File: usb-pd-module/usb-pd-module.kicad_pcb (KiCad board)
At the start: 2 copper layers, 34.3 x 46.3 mm, 33 parts, among them J1 USBC, J2 OUT, U1 CH221K, U2 SPX1117M3

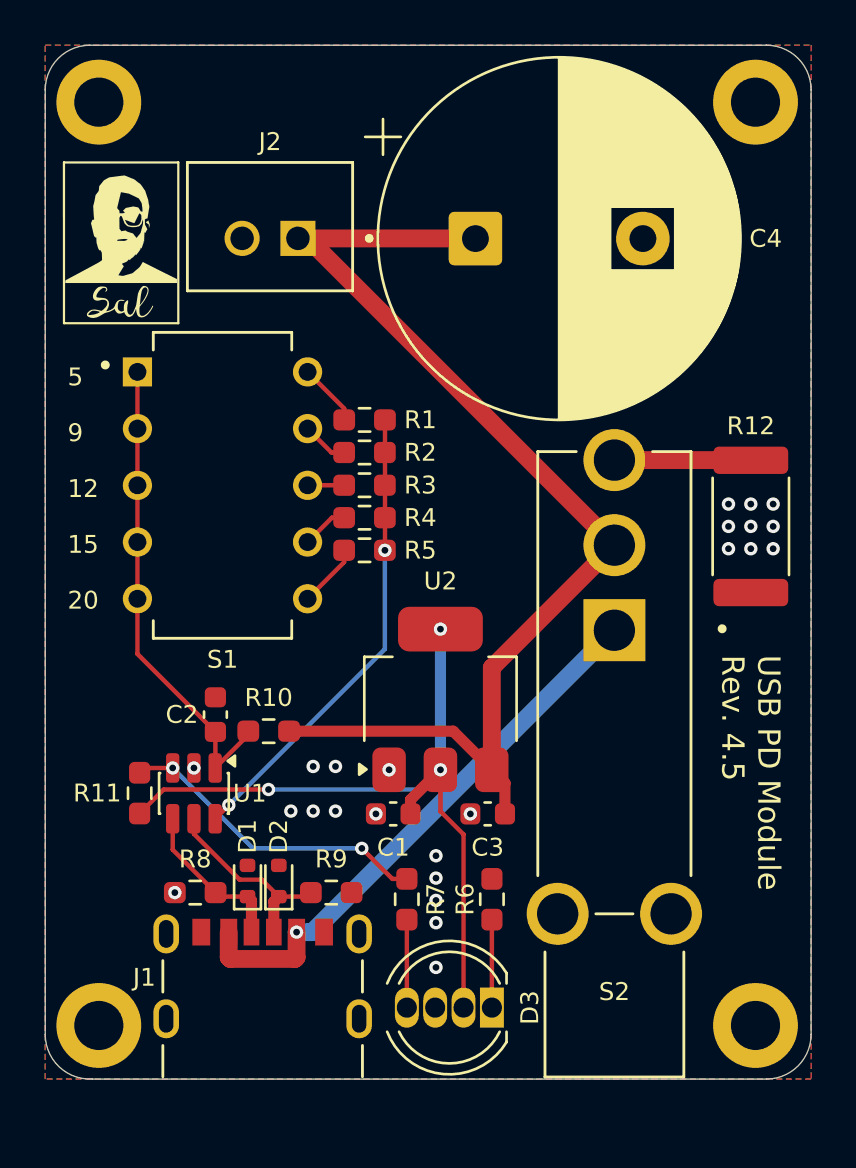
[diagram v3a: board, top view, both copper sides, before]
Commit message: Adjust USB-C connector and main switch placement for better enclosure compatibility
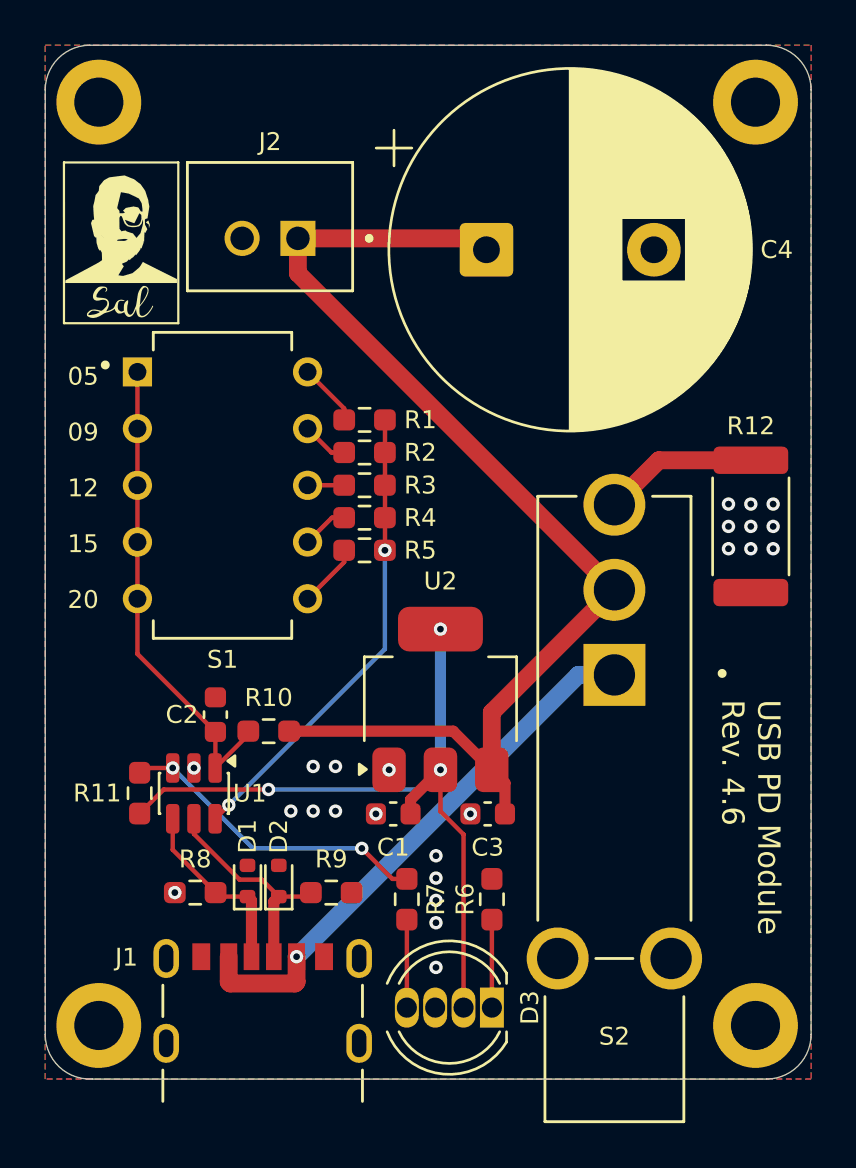
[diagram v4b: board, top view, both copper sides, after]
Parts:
- moved REF** 2.00 mm to (59.6, 76.2)
- moved REF** 2.00 mm to (50.6, 76.0)
- moved S2 2.00 mm to (60.5, 66.1)
- moved J1 1.10 mm to (44.7, 85.5)
- moved C4 0.70 mm to (54.8, 50.9)
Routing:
- net CC1: track 7.27 -> 8.37 mm
- net CC2: track 8.84 -> 9.94 mm
- net BLEED: track 6.11 -> 6.95 mm
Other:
- board text added: "05"
- board text added: "09"
- board text added: "USB PD Module Rev. 4.6"
- board text removed: "5"
- board text removed: "9"
- board text removed: "USB PD Module Rev. 4.5"
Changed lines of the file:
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@@
 	(title_block
 		(title "USB PD Module PCB")
-		(date "2026-03-21")
-		(rev "4.5")
+		(date "2026-05-27")
+		(rev "4.6")
 		(company "Salinder Sidhu")
 	)
@@
 	(footprint "footprints:SW_100SP1T2B4M7QE"
 		(layer "F.Cu")
-		(at 60.49 64.09 90)
+		(at 60.49 66.09 90)
 		(property "Reference" "S2"
 			(at -20 0 180)
@@
 	(footprint "footprints:AMPHENOL_10164359-00011LF"
 		(layer "F.Cu")
-		(at 44.7375 84.45)
+		(at 44.7375 85.55)
 		(property "Reference" "J1"
-			(at -5.3 -1 0)
+			(at -6.1 -3 0)
 			(layer "F.SilkS")
 			(effects
@@
 	(footprint "Capacitor_THT:CP_Radial_D16.0mm_P7.50mm"
 		(layer "F.Cu")
-		(at 54.267246 50.36)
+		(at 54.76 50.86)
 		(descr "CP, Radial series, Radial, pin pitch=7.50mm, diameter=16mm, height=25mm, Electrolytic Capacitor")
 		(tags "CP Radial series Radial pin pitch 7.50mm diameter 16mm height 25mm Electrolytic Capacitor")
@@
 	(footprint "Symbol:WEEE-Logo_4.2x6mm_SilkScreen"
 		(layer "B.Cu")
-		(at 59.57 74.21 180)
+		(at 59.57 76.21 180)
 		(descr "Waste Electrical and Electronic Equipment Directive https://eur-lex.europa.eu/legal-content/EN/TXT/PDF/?uri=CELEX:32012L0019#page=29")
 		(tags "Logo WEEE")
@@
 	(footprint "Symbol:KiCad-Logo2_5mm_SilkScreen"
 		(layer "B.Cu")
-		(at 50.57 73.96 180)
+		(at 50.57 75.96 180)
 		(descr "KiCad Logo")
 		(tags "Logo KiCad")
@@
 		(layer "Edge.Cuts")
 	)
-	(gr_text "5"
-		(at 36 57.03 0)
+	(gr_text "05"
+		(at 36 57 0)
 		(layer "F.SilkS")
 		(effects
@@
 		)
 	)
-	(gr_text "9"
-		(at 36 59.53 0)
+	(gr_text "09"
+		(at 36 59.5 0)
 		(layer "F.SilkS")
 		(effects
@@
 	)
 	(gr_text "12"
-		(at 36 62.03 0)
+		(at 36 62 0)
 		(layer "F.SilkS")
 		(effects
@@
 	)
 	(gr_text "15"
-		(at 36 64.53 0)
+		(at 36 64.5 0)
 		(layer "F.SilkS")
 		(effects
@@
 	)
 	(gr_text "20"
-		(at 36 67.03 0)
+		(at 36 67 0)
 		(layer "F.SilkS")
 		(effects
@@
 		)
 	)
-	(gr_text "USB PD Module\nRev. 4.5"
-		(at 65.2 69 270)
+	(gr_text "USB PD Module\nRev. 4.6"
+		(at 65.2 71 270)
 		(layer "F.SilkS")
 		(effects
@@
 	)
 	(segment
+		(start 45.2375 82.52)
+		(end 45.2375 80.0525)
+		(width 0.5)
+		(layer "F.Cu")
+		(net "CC2")
+	)
+	(segment
 		(start 46.7175 79.83)
 		(end 46.8975 79.65)
@@
 	)
 	(segment
-		(start 41.66 77.021968)
-		(end 41.66 76.34375)
-		(width 0.2)
+		(start 45.2375 80.0525)
+		(end 45.46 79.83)
+		(width 0.5)
 		(layer "F.Cu")
 		(net "CC2")
 	)
 	(segment
-		(start 45.2375 81.42)
-		(end 45.2375 80.0525)
-		(width 0.5)
+		(start 41.66 77.021968)
+		(end 41.66 76.34375)
+		(width 0.2)
 		(layer "F.Cu")
 		(net "CC2")
@@
 		(net "CC2")
 	)
-	(segment
-		(start 45.2375 80.0525)
-		(end 45.46 79.83)
-		(width 0.5)
-		(layer "F.Cu")
-		(net "CC2")
-	)
 	(via
 		(at 50.4 74.15)
@@
 	)
 	(segment
-		(start 46.2575 81.42)
-		(end 46.2575 82.552)
+		(start 46.2575 83.65)
+		(end 46.1875 83.72)
 		(width 0.8)
 		(layer "F.Cu")
@@
 	)
 	(segment
-		(start 43.2175 82.552)
-		(end 43.2175 81.42)
+		(start 46.2575 82.52)
+		(end 46.2575 83.65)
 		(width 0.8)
 		(layer "F.Cu")
@@
 	)
 	(segment
-		(start 43.2865 82.621)
-		(end 43.2175 82.552)
+		(start 43.2875 83.72)
+		(end 43.2175 83.65)
 		(width 0.8)
 		(layer "F.Cu")
@@
 	)
 	(segment
-		(start 46.1885 82.621)
-		(end 43.2865 82.621)
+		(start 43.2175 83.65)
+		(end 43.2175 82.52)
 		(width 0.8)
 		(layer "F.Cu")
@@
 	)
 	(segment
-		(start 46.2575 82.552)
-		(end 46.1885 82.621)
+		(start 46.1875 83.72)
+		(end 43.2875 83.72)
 		(width 0.8)
 		(layer "F.Cu")
@@
 	)
 	(via
-		(at 46.2575 81.42)
+		(at 46.2575 82.52)
 		(size 0.6)
 		(drill 0.3)
 		(layers "F.Cu" "B.Cu")
-		(capping no)
-		(covering
-			(front no)
-			(back no)
-		)
-		(plugging
-			(front no)
-			(back no)
-		)
-		(filling no)
 		(net "VBUS")
 	)
 	(segment
-		(start 46.2575 81.42)
-		(end 46.97 81.42)
+		(start 58.8775 69.9)
+		(end 60.49 69.9)
 		(width 0.8)
 		(layer "B.Cu")
@@
 	)
 	(segment
-		(start 46.97 81.42)
-		(end 60.49 67.9)
+		(start 46.2575 82.52)
+		(end 58.8775 69.9)
 		(width 0.8)
 		(layer "B.Cu")
@@
 	)
 	(segment
-		(start 47 50.6)
-		(end 47 50.35)
+		(start 54.25 50.35)
+		(end 54.76 50.86)
+		(width 0.8)
+		(layer "F.Cu")
+		(net "PWR")
+	)
+	(segment
+		(start 46.3175 51.9175)
+		(end 60.49 66.09)
 		(width 0.8)
 		(layer "F.Cu")
@@
 	)
 	(segment
-		(start 60.49 64.09)
-		(end 46.75 50.35)
+		(start 60.49 66.09)
+		(end 55 71.58)
 		(width 0.8)
 		(layer "F.Cu")
@@
 	)
 	(segment
-		(start 55 69.58)
-		(end 55 74.15)
+		(start 46.3175 50.35)
+		(end 46.3175 51.9175)
 		(width 0.8)
 		(layer "F.Cu")
@@
 	)
 	(segment
-		(start 46.75 50.35)
-		(end 46.3175 50.35)
+		(start 46.3175 50.35)
+		(end 54.25 50.35)
 		(width 0.8)
 		(layer "F.Cu")
@@
 	)
 	(segment
-		(start 46.3175 50.35)
-		(end 54.257246 50.35)
-		(width 0.8)
-		(layer "F.Cu")
-		(net "PWR")
-	)
-	(segment
-		(start 54.257246 50.35)
-		(end 54.267246 50.36)
-		(width 0.8)
-		(layer "F.Cu")
-		(net "PWR")
-	)
-	(segment
 		(start 55.59 76.125)
 		(end 55.59 74.74)
@@
 	)
 	(segment
-		(start 60.49 64.09)
-		(end 55 69.58)
+		(start 55 71.58)
+		(end 55 74.15)
 		(width 0.8)
 		(layer "F.Cu")
@@
 	)
 	(segment
-		(start 60.49 60.28)
-		(end 66.5925 60.28)
+		(start 66.6 60.2875)
+		(end 62.4825 60.2875)
+		(width 0.8)
+		(layer "F.Cu")
+		(net "BLEED")
+	)
+	(segment
+		(start 62.4825 60.2875)
+		(end 60.49 62.28)
 		(width 0.8)
 		(layer "F.Cu")
@@
 	)
 	(segment
-		(start 44.2375 81.42)
-		(end 44.2375 80.0075)
-		(width 0.5)
-		(layer "F.Cu")
-		(net "CC1")
-	)
-	(segment
-		(start 44.2375 80.0075)
-		(end 44.06 79.83)
-		(width 0.5)
-		(layer "F.Cu")
-		(net "CC1")
-	)
-	(segment
 		(start 40.71 77.73)
 		(end 40.71 76.34375)
@@
 	)
 	(segment
+		(start 44.2375 82.52)
+		(end 44.2375 80.0075)
+		(width 0.5)
+		(layer "F.Cu")
+		(net "CC1")
+	)
+	(segment
 		(start 42.81 79.83)
 		(end 42.63 79.65)
@@
 		(layer "F.Cu")
 		(net "CC1")
+	)
+	(segment
+		(start 44.2375 80.0075)
+		(end 44.06 79.83)
+		(width 0.5)
+		(layer "F.Cu")
+		(net "CC1")
